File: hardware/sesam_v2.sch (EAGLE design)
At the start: 11 parts, among them X2 C-GRID-06-70543

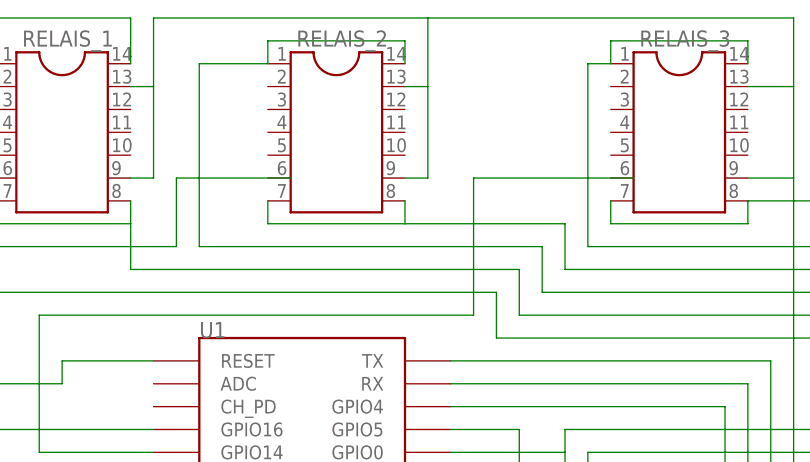
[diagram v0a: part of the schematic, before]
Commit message: new layout, all non smd components mirrored
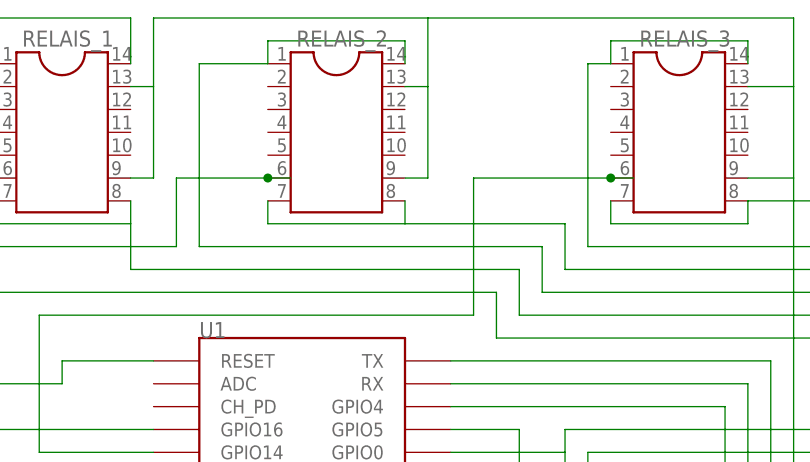
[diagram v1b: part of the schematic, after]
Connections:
- net N$14: now also RELAIS_2.6
- net N$15: now also RELAIS_3.6
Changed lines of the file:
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@@
 <grid distance="0.1" unitdist="inch" unit="inch" style="lines" multiple="1" display="no" altdistance="0.01" altunitdist="inch" altunit="inch"/>
 <layers>
-<layer number="1" name="Top" color="4" fill="1" visible="yes" active="no"/>
-<layer number="16" name="Bottom" color="1" fill="1" visible="yes" active="no"/>
-<layer number="17" name="Pads" color="2" fill="1" visible="yes" active="no"/>
-<layer number="18" name="Vias" color="2" fill="1" visible="yes" active="no"/>
-<layer number="19" name="Unrouted" color="6" fill="1" visible="yes" active="no"/>
-<layer number="20" name="Dimension" color="15" fill="1" visible="yes" active="no"/>
-<layer number="21" name="tPlace" color="7" fill="1" visible="yes" active="no"/>
-<layer number="22" name="bPlace" color="7" fill="1" visible="yes" active="no"/>
-<layer number="23" name="tOrigins" color="15" fill="1" visible="yes" active="no"/>
-<layer number="24" name="bOrigins" color="15" fill="1" visible="yes" active="no"/>
-<layer number="25" name="tNames" color="7" fill="1" visible="yes" active="no"/>
-<layer number="26" name="bNames" color="7" fill="1" visible="yes" active="no"/>
-<layer number="27" name="tValues" color="7" fill="1" visible="yes" active="no"/>
-<layer number="28" name="bValues" color="7" fill="1" visible="yes" active="no"/>
+<layer number="1" name="Top" color="4" fill="1" visible="no" active="no"/>
+<layer number="16" name="Bottom" color="1" fill="1" visible="no" active="no"/>
+<layer number="17" name="Pads" color="2" fill="1" visible="no" active="no"/>
+<layer number="18" name="Vias" color="2" fill="1" visible="no" active="no"/>
+<layer number="19" name="Unrouted" color="6" fill="1" visible="no" active="no"/>
+<layer number="20" name="Dimension" color="15" fill="1" visible="no" active="no"/>
+<layer number="21" name="tPlace" color="7" fill="1" visible="no" active="no"/>
+<layer number="22" name="bPlace" color="7" fill="1" visible="no" active="no"/>
+<layer number="23" name="tOrigins" color="15" fill="1" visible="no" active="no"/>
+<layer number="24" name="bOrigins" color="15" fill="1" visible="no" active="no"/>
+<layer number="25" name="tNames" color="7" fill="1" visible="no" active="no"/>
+<layer number="26" name="bNames" color="7" fill="1" visible="no" active="no"/>
+<layer number="27" name="tValues" color="7" fill="1" visible="no" active="no"/>
+<layer number="28" name="bValues" color="7" fill="1" visible="no" active="no"/>
 <layer number="29" name="tStop" color="7" fill="3" visible="no" active="no"/>
 <layer number="30" name="bStop" color="7" fill="6" visible="no" active="no"/>
@@
 <layer number="35" name="tGlue" color="7" fill="4" visible="no" active="no"/>
 <layer number="36" name="bGlue" color="7" fill="5" visible="no" active="no"/>
-<layer number="37" name="tTest" color="7" fill="1" visible="yes" active="no"/>
-<layer number="38" name="bTest" color="7" fill="1" visible="yes" active="no"/>
+<layer number="37" name="tTest" color="7" fill="1" visible="no" active="no"/>
+<layer number="38" name="bTest" color="7" fill="1" visible="no" active="no"/>
 <layer number="39" name="tKeepout" color="4" fill="11" visible="no" active="no"/>
 <layer number="40" name="bKeepout" color="1" fill="11" visible="no" active="no"/>
@@
 <layer number="44" name="Drills" color="7" fill="1" visible="no" active="no"/>
 <layer number="45" name="Holes" color="7" fill="1" visible="no" active="no"/>
-<layer number="46" name="Milling" color="3" fill="1" visible="yes" active="no"/>
-<layer number="47" name="Measures" color="7" fill="1" visible="yes" active="no"/>
-<layer number="48" name="Document" color="7" fill="1" visible="yes" active="no"/>
-<layer number="49" name="Reference" color="7" fill="1" visible="yes" active="no"/>
-<layer number="51" name="tDocu" color="7" fill="1" visible="yes" active="no"/>
-<layer number="52" name="bDocu" color="7" fill="1" visible="yes" active="no"/>
+<layer number="46" name="Milling" color="3" fill="1" visible="no" active="no"/>
+<layer number="47" name="Measures" color="7" fill="1" visible="no" active="no"/>
+<layer number="48" name="Document" color="7" fill="1" visible="no" active="no"/>
+<layer number="49" name="Reference" color="7" fill="1" visible="no" active="no"/>
+<layer number="51" name="tDocu" color="7" fill="1" visible="no" active="no"/>
+<layer number="52" name="bDocu" color="7" fill="1" visible="no" active="no"/>
 <layer number="90" name="Modules" color="5" fill="1" visible="yes" active="yes"/>
 <layer number="91" name="Nets" color="2" fill="1" visible="yes" active="yes"/>
@@
 <wire x1="66.04" y1="76.2" x2="86.36" y2="76.2" width="0.1524" layer="91"/>
 <wire x1="86.36" y1="76.2" x2="86.36" y2="83.82" width="0.1524" layer="91"/>
-<wire x1="86.36" y1="83.82" x2="99.06" y2="83.82" width="0.1524" layer="91"/>
+<wire x1="86.36" y1="83.82" x2="96.52" y2="83.82" width="0.1524" layer="91"/>
+<pinref part="RELAIS_2" gate="G$1" pin="6"/>
+<wire x1="96.52" y1="83.82" x2="99.06" y2="83.82" width="0.1524" layer="91"/>
+<junction x="96.52" y="83.82"/>
 </segment>
 </net>
@@
 <wire x1="71.12" y1="68.58" x2="119.38" y2="68.58" width="0.1524" layer="91"/>
 <wire x1="119.38" y1="68.58" x2="119.38" y2="83.82" width="0.1524" layer="91"/>
-<wire x1="119.38" y1="83.82" x2="137.16" y2="83.82" width="0.1524" layer="91"/>
-</segment>
-</net>
+<wire x1="119.38" y1="83.82" x2="134.62" y2="83.82" width="0.1524" layer="91"/>
+<pinref part="RELAIS_3" gate="G$1" pin="6"/>
+<wire x1="134.62" y1="83.82" x2="137.16" y2="83.82" width="0.1524" layer="91"/>
+<junction x="134.62" y="83.82"/>
+</segment>
+</net>
